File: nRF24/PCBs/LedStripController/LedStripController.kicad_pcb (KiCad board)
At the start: 2 copper layers, 88.5 x 38 mm, 13 parts, among them M1 TP4056, U1 NRF24L01, U2 ATtiny84, U3 MCP1700x-330

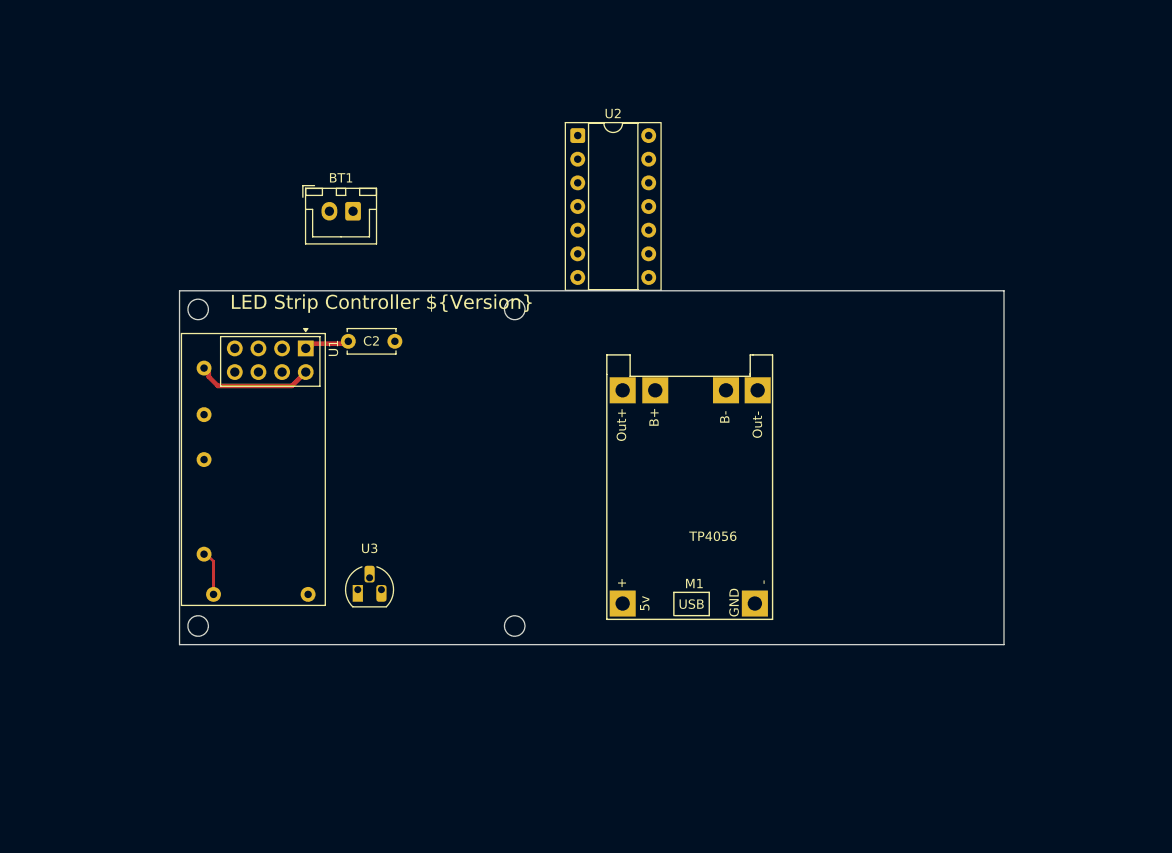
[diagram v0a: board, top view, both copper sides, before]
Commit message: LED Strip Controller and Programming Adapter WIP
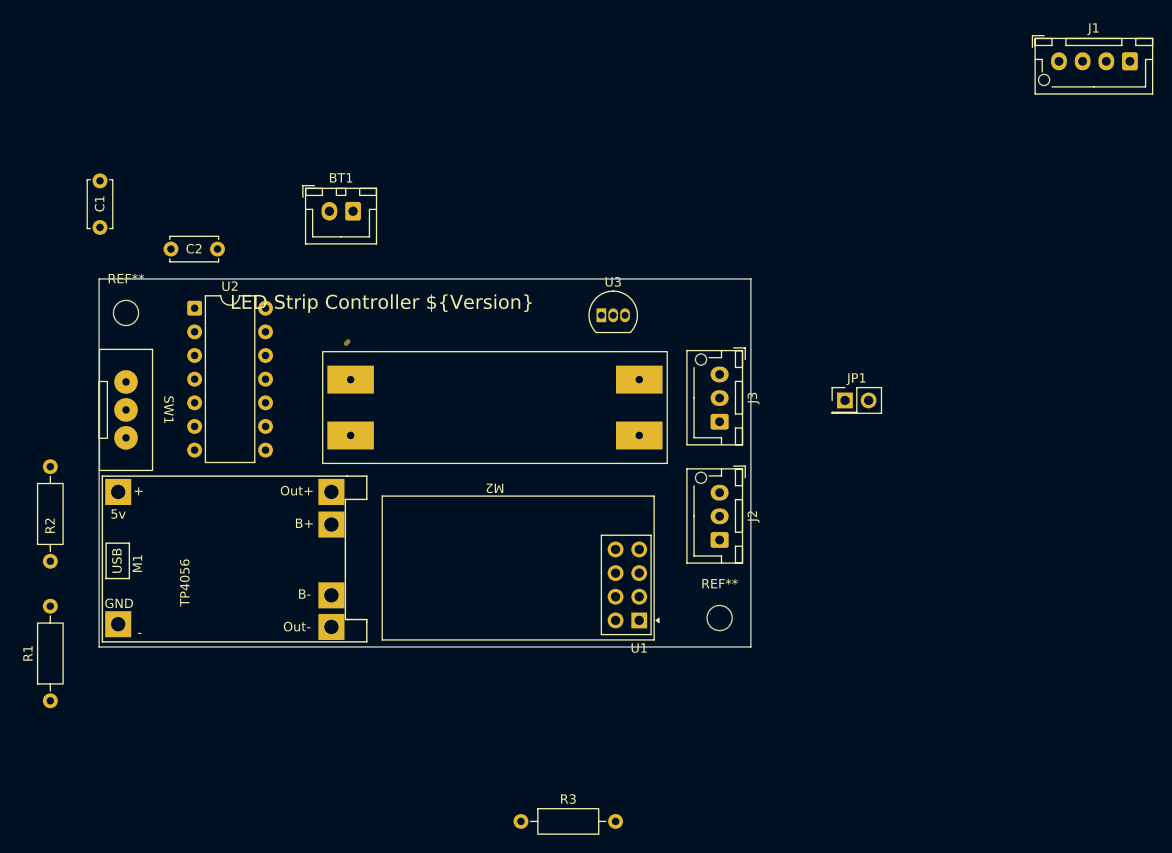
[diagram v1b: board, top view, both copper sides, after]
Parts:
- removed the REF** at (153.0, 137.0)
- removed the REF** at (119.0, 137.0)
- removed the REF** at (119.0, 103.0)
- removed the REF** at (153.0, 103.0)
- added J1: Prog, hagego:JST_XH_1x04_P2.54, F.Cu at (211.4, 76.4)
- added J2: WS2812 1, hagego:JST_XH_1x03_P2.54, F.Cu at (175.0, 122.7)
- added J3: WS2812 2, hagego:JST_XH_1x03_P2.54, F.Cu at (175.0, 110.0)
- added JP1: Jumper CSN, Connector_PinHeader_2.54mm:PinHeader_2x01_P2.54mm_Vertical, F.Cu at (188.5, 112.8)
- added M2: ~, hagego:MT3608_Module, F.Cu at (150.9, 113.5)
- added R3: 1M, Resistor_THT:R_Axial_DIN0207_L6.3mm_D2.5mm_P10.16mm_Horizontal, F.Cu at (153.7, 158.0)
- added REF**: MountingHole_2.7mm, MountingHole:MountingHole_2.7mm, F.Cu at (111.3, 103.4)
- added REF**: MountingHole_2.7mm, MountingHole:MountingHole_2.7mm, F.Cu at (175.0, 136.1)
- added SW1: on/off, hagego:SwitchHorizontal_SK-12F14, F.Cu at (111.3, 113.8)
- C1, R1, R2: moved to F.Cu
- U2: footprint Package_DIP:DIP-14_W7.62mm_Socket -> Package_DIP:DIP-14_W7.62mm
- U3: footprint Package_TO_SOT_THT:TO-92_HandSolder -> Package_TO_SOT_THT:TO-92_Inline
- moved M1 56.3 mm to (108.7, 120.9), turned to 0 degrees
- moved U1 46.2 mm to (166.4, 136.4), turned to 180 degrees
- moved U2 45.1 mm to (118.6, 102.9)
- moved U3 39.4 mm to (162.3, 103.6)
- moved R1 30.0 mm to (103.1, 145.0), turned to 90 degrees
- moved C1 23.0 mm to (108.5, 94.2)
- moved C2 21.5 mm to (116.1, 96.5)
- moved R2 16.5 mm to (103.1, 130.0)
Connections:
- M1 pad 5: +3V8 -> Net-(M1-B+)
- U1 pad 4: Net-(U1-~{CSN}) -> Net-(JP1-B)
- U2 pad 10: unconnected-(U2-PA3-Pad10) -> Net-(J3-Pin_3)
- U2 pad 4: unconnected-(U2-~{RESET}/PB3-Pad4) -> Net-(J1-Pin_1)
- U2 pad 5: Net-(U1-~{CSN}) -> Net-(JP1-A)
- U2 pad 6: unconnected-(U2-PA7-Pad6) -> Net-(J2-Pin_3)
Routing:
- net /VCC: track 12.6 -> 0.00 mm
- net GND: track 5.75 -> 0.36 mm
- net Net-(U2-AREF/PA0): track 4.89 -> 0.00 mm
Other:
- board size 88.5 x 38 mm -> 70 x 39.5 mm

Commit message: LED Strip Coller WIP
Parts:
- removed REF** (x2): MountingHole_2.7mm, MountingHole:MountingHole_2.7mm
- added H: M2.5, MountingHole:MountingHole_2.7mm_M2.5, F.Cu at (171.0, 103.0)
- added H: 5mm, hagego:Hole_5mm, F.Cu at (113.0, 141.0)
- added H: 5mm, hagego:Hole_5mm, F.Cu at (177.0, 141.0)
- added H: 5mm, hagego:Hole_5mm, F.Cu at (177.0, 103.0)
- added H: 5mm, hagego:Hole_5mm, F.Cu at (113.0, 103.0)
- added H: M2.5, MountingHole:MountingHole_2.7mm_M2.5, F.Cu at (119.0, 103.0)
- added H: M2.5, MountingHole:MountingHole_2.7mm_M2.5, F.Cu at (171.0, 141.0)
- added H: M2.5, MountingHole:MountingHole_2.7mm_M2.5, F.Cu at (119.0, 141.0)
- moved J1 104.8 mm to (128.8, 140.7)
- moved R2 52.6 mm to (155.7, 132.6), turned to 180 degrees
- moved JP1 47.1 mm to (150.9, 141.2)
- moved R1 43.4 mm to (145.5, 135.9), turned to 0 degrees
- moved C1 42.8 mm to (150.6, 101.6), turned to 180 degrees
- moved C2 30.5 mm to (145.3, 105.4)
- moved R3 30.0 mm to (145.8, 129.0)
- moved BT1 12.2 mm to (138.9, 103.1)
- moved U3 8.38 mm to (153.9, 103.5)
- moved U2 6.36 mm to (125.0, 102.6)
- moved J3 3.66 mm to (177.0, 113.0)
- moved J2 3.31 mm to (176.8, 125.5)
- moved M2 2.59 mm to (153.4, 114.0)
- moved SW1 2.05 mm to (113.0, 112.8)
- moved M1 1.83 mm to (110.2, 119.9)
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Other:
- board size 70 x 39.5 mm -> 70 x 44 mm

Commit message: LED Strip Controller production version
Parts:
- removed H (x4): M2.5, MountingHole:MountingHole_2.7mm_M2.5
- removed H (x4): 5mm, hagego:Hole_5mm
- added D1: LED, LED_THT:LED_D3.0mm, F.Cu at (179.2, 119.0)
- added J4: Bat 2, hagego:JST_XH_1x02_P2.54, F.Cu at (164.9, 140.7)
- added R4: 100, Resistor_THT:R_Axial_DIN0207_L6.3mm_D2.5mm_P10.16mm_Horizontal, B.Cu at (167.2, 133.3)
- added REF**: 2.7mm, MountingHole:MountingHole_2.7mm_M2.5, F.Cu at (120.0, 100.5)
- added REF**: 5mm, MountingHole:MountingHole_5mm, F.Cu at (113.5, 100.5)
- added REF**: 5mm, MountingHole:MountingHole_5mm, F.Cu at (178.5, 100.5)
- added REF**: 5mm, MountingHole:MountingHole_5mm, F.Cu at (113.5, 140.5)
- added REF**: 2.7mm, MountingHole:MountingHole_2.7mm_M2.5, F.Cu at (174.0, 120.5)
- added REF**: 2.7mm, MountingHole:MountingHole_2.7mm_M2.5, F.Cu at (120.0, 140.5)
- added REF**: 5mm, MountingHole:MountingHole_5mm, F.Cu at (178.5, 140.5)
- Bat1: renamed from BT1; footprint hagego:JST_XH_1x02_P2.54 -> hagego:JST_PH_1x02_P2.00
- J1: footprint hagego:JST_XH_1x04_P2.54 -> Connector_PinHeader_2.54mm:PinHeader_1x04_P2.54mm_Vertical
- R1, R2, R3: moved to B.Cu
- U3: footprint Package_TO_SOT_THT:TO-92_Inline -> Package_TO_SOT_THT:TO-92_HandSolder
- moved Bat1 40.4 mm to (151.7, 141.5), turned to 180 degrees
- moved U3 34.9 mm to (119.1, 106.9)
- moved C1 30.2 mm to (122.4, 112.2)
- moved C2 29.8 mm to (117.4, 116.1)
- moved U1 29.0 mm to (142.1, 122.5), turned to 0 degrees
- moved R1 18.2 mm to (159.5, 124.2), turned to 180 degrees
- moved R3 14.2 mm to (159.5, 132.6), turned to 180 degrees
- moved JP1 11.7 mm to (139.2, 141.7)
- moved R2 7.53 mm to (149.4, 128.5), turned to 0 degrees
- moved M2 5.75 mm to (153.8, 108.3)
- moved J1 4.17 mm to (124.7, 141.7), turned to 90 degrees
- moved J3 3.95 mm to (178.8, 109.5)
- moved J2 2.26 mm to (178.8, 126.5)
- moved SW1 1.70 mm to (113.0, 111.1)
- moved U2 1.07 mm to (125.2, 101.6)
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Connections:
- net Net-(J1-Pin_2) renamed /MOSI
- net Net-(J1-Pin_3) renamed /MISO
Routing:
- net GND: track 0.36 -> 188.8 mm
- net /VCC: track 0.00 -> 81.0 mm
- net +3V8: track 0.00 -> 75.3 mm
- net /Vbat: track 0.00 -> 71.6 mm, vias 0 -> 1
- net Net-(M1-B+): track 0.00 -> 68.4 mm, vias 0 -> 1
- net Net-(J2-Pin_3): track 0.00 -> 67.5 mm, vias 0 -> 2
- net /MOSI: track 0.00 -> 63.9 mm, vias 0 -> 1
- net Net-(J3-Pin_3): track 0.00 -> 53.7 mm, vias 0 -> 1
- net /MISO: track 0.00 -> 49.9 mm, vias 0 -> 1
- net Net-(J1-Pin_4): track 0.00 -> 41.2 mm, vias 0 -> 1
- net Net-(U2-AREF/PA0): track 0.00 -> 39.0 mm
- net Net-(J1-Pin_1): track 0.00 -> 37.2 mm, vias 0 -> 2
- net Net-(JP1-A): track 0.00 -> 36.6 mm, vias 0 -> 1
- net /VLED: track 0.00 -> 30.2 mm
- net Net-(U1-CE): track 0.00 -> 29.4 mm
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- added copper zone on B.Cu, net (none)
- added copper zone on F.Cu, net (none)
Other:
- board size 70 x 44 mm -> 72 x 47 mm
- board text added: "LED Strip ${Version}"
- board text removed: "LED Strip Controller ${Version}"

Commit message: nRF24 LED Strip Controller Debugging
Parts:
- removed JP1: Jumper CSN, Connector_PinHeader_2.54mm:PinHeader_2x01_P2.54mm_Vertical
- renumbered J4 to Bat2
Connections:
- R3 pad 2: Net-(JP1-B) -> Net-(U1-~{CSN})
- U1 pad 4: Net-(JP1-B) -> Net-(U1-~{CSN})
- U1 pad 5: Net-(J1-Pin_4) -> Net-(J1-Pin_1)
- U2 pad 4: Net-(J1-Pin_1) -> Net-(J1-Pin_4)
- U2 pad 5: Net-(JP1-A) -> Net-(U1-~{CSN})
- U2 pad 9: Net-(J1-Pin_4) -> Net-(J1-Pin_1)
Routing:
- net Net-(J1-Pin_4): track 41.2 -> 0.00 mm, vias 1 -> 0
- net Net-(JP1-A): track 36.6 -> 0.00 mm, vias 1 -> 0
- net Net-(JP1-B): track 22.2 -> 0.00 mm
- net Net-(J1-Pin_1): track 37.2 -> 18.1 mm, vias 2 -> 0
- net Net-(U1-~{CSN}): track 0.00 -> 9.86 mm
- removed copper zone on B.Cu, net (none)
- removed copper zone on F.Cu, net (none)
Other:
- board text added: "+"
